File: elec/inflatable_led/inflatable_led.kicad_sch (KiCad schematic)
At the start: 87 parts, among them J1 Header-Male-2.54_1x20, J2 Conn_01x02_Pin, J3 Conn_01x02_Pin, SW1 TS-1093C-A7B2-D1, U1 RP2040, U2 W25Q128JVSIQTR, U3 TPS61165DRVR, U4 BQ24040DSQR, U5 AMS1117-3.3, U6 F.0603.00026/P2-0603B1TS2-06T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, U7 SI2323DS, X1 X322512MSB4SI

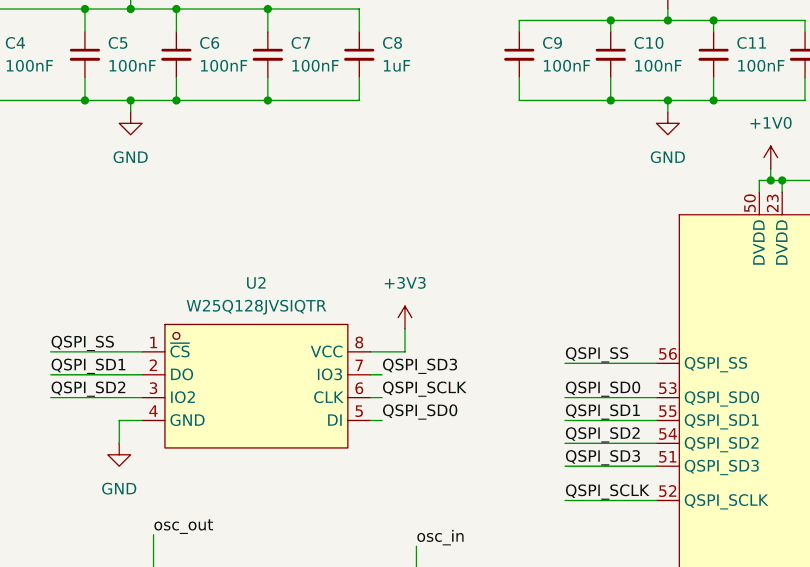
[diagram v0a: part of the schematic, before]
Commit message: fix missing 3.3V on flash
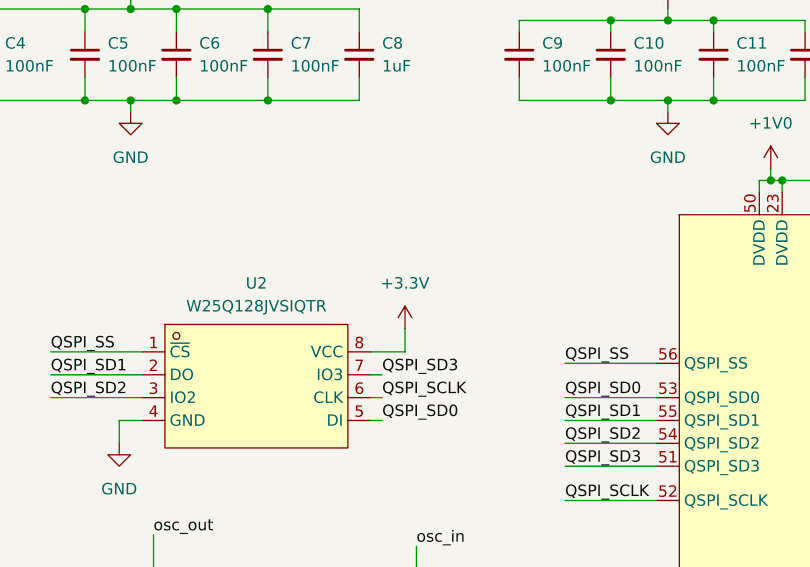
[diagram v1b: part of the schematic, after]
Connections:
- net +3V3 is gone; now on net +3.3V: U2.8 (VCC)
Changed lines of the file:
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@@
+	)
+	(symbol
+		(lib_id "power:+3.3V")
+		(at 85.09 62.23 0)
+		(unit 1)
+		(exclude_from_sim no)
+		(in_bom yes)
+		(on_board yes)
+		(dnp no)
+		(fields_autoplaced yes)
+		(property "Reference" "#PWR09"
+			(at 85.09 66.04 0)
+			(effects
+				(font
+					(size 1.27 1.27)
+				)
+				(hide yes)
+			)
+		)
+		(property "Value" "+3.3V"
+			(at 85.09 57.15 0)
+			(effects
+				(font
+					(size 1.27 1.27)
+				)
+			)
+		)
+		(property "Footprint" ""
+			(at 85.09 62.23 0)
+			(effects
+				(font
+					(size 1.27 1.27)
+				)
+				(hide yes)
+			)
+		)
+		(property "Datasheet" ""
+			(at 85.09 62.23 0)
+			(effects
+				(font
+					(size 1.27 1.27)
+				)
+				(hide yes)
+			)
+		)
+		(property "Description" "Power symbol creates a global label with name \"+3.3V\""
+			(at 85.09 62.23 0)
+			(effects
+				(font
+					(size 1.27 1.27)
+				)
+				(hide yes)
+			)
+		)
+		(pin "1"
+		)
+		(instances
+			(project "inflatable_led"
+				(path "/28d8f95b-9544-4a45-87c6-73291c5b1588"
+					(reference "#PWR09")
+					(unit 1)
+				)
+			)
+		)
 	)
 	(symbol
@@
 					(unit 1)
 				)
-			)
-		)
-	)
-	(symbol
-		(lib_id "power:+3V3")
-		(at 85.09 62.23 0)
-		(unit 1)
-		(exclude_from_sim no)
-		(in_bom yes)
-		(on_board yes)
-		(dnp no)
-		(fields_autoplaced yes)
-		(property "Reference" "#PWR09"
-			(at 85.09 66.04 0)
-			(effects
-				(font
-					(size 1.27 1.27)
-				)
-				(hide yes)
-			)
-		)
-		(property "Value" "+3V3"
-			(at 85.09 57.15 0)
-			(effects
-				(font
-					(size 1.27 1.27)
-				)
-			)
-		)
-		(property "Footprint" ""
-			(at 85.09 62.23 0)
-			(effects
-				(font
-					(size 1.27 1.27)
-				)
-				(hide yes)
-			)
-		)
-		(property "Datasheet" ""
-			(at 85.09 62.23 0)
-			(effects
-				(font
-					(size 1.27 1.27)
-				)
-				(hide yes)
-			)
-		)
-		(property "Description" "Power symbol creates a global label with name \"+3V3\""
-			(at 85.09 62.23 0)
-			(effects
-				(font
-					(size 1.27 1.27)
-				)
-				(hide yes)
-			)
-		)
-		(pin "1"
-		)
-		(instances
-			(project "inflatable_led"
-				(path "/28d8f95b-9544-4a45-87c6-73291c5b1588"
-					(reference "#PWR09")
-					(unit 1)
-				)

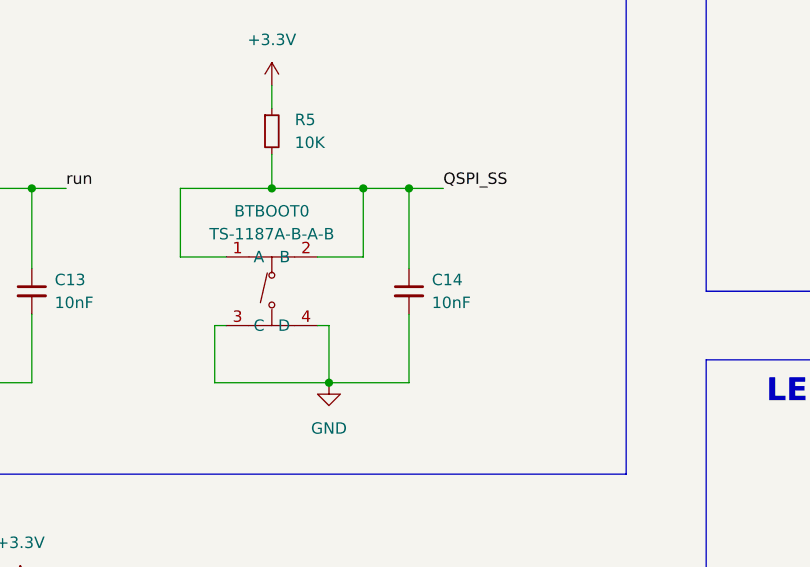
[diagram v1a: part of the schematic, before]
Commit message: v1 is working, add v2 requests
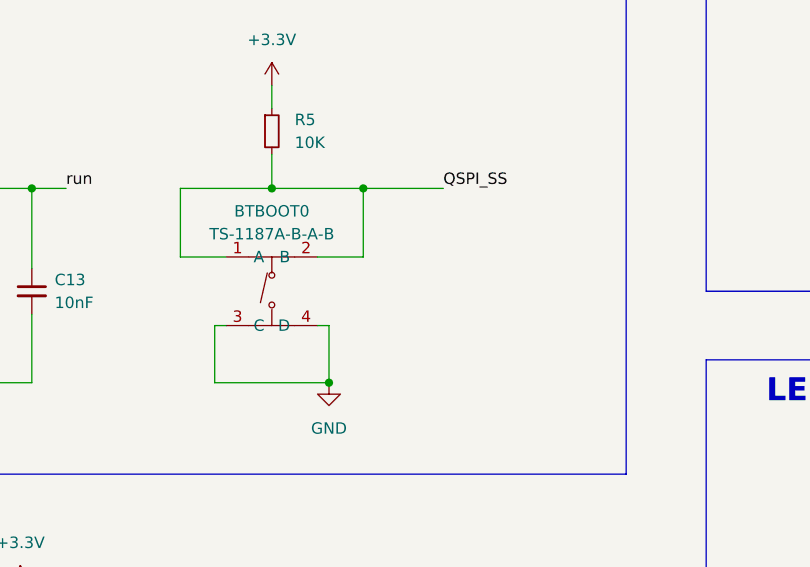
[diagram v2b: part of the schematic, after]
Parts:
- removed C14: 10nF, Capacitor_SMD:C_0402_1005Metric, symbol Device:C_Small
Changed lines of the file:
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@@
 	)
 	(junction
-		(at 181.61 179.07)
-		(diameter 0)
-		(color 0 0 0 0)
-	)
-	(junction
 		(at 157.48 45.72)
 		(diameter 0)
@@
 	(wire
 		(pts
-			(xy 181.61 193.04) (xy 181.61 200.66)
-		)
-		(stroke
-			(width 0)
-			(type default)
-		)
-	)
-	(wire
-		(pts
 			(xy 276.86 165.1) (xy 276.86 167.64)
 		)
@@
 	(wire
 		(pts
-			(xy 176.53 179.07) (xy 181.61 179.07)
+			(xy 176.53 179.07) (xy 185.42 179.07)
 		)
 		(stroke
@@
 	(wire
 		(pts
-			(xy 181.61 179.07) (xy 185.42 179.07)
-		)
-		(stroke
-			(width 0)
-			(type default)
-		)
-	)
-	(wire
-		(pts
 			(xy 102.87 77.47) (xy 113.03 77.47)
 		)
@@
 	(wire
 		(pts
-			(xy 181.61 200.66) (xy 172.72 200.66)
-		)
-		(stroke
-			(width 0)
-			(type default)
-		)
-	)
-	(wire
-		(pts
 			(xy 80.01 115.57) (xy 72.39 115.57)
 		)
@@
 	(wire
 		(pts
-			(xy 181.61 179.07) (xy 181.61 187.96)
-		)
-		(stroke
-			(width 0)
-			(type default)
-		)
-	)
-	(wire
-		(pts
 			(xy 189.23 130.81) (xy 195.58 130.81)
 		)
@@
 					(unit 1)
 				)
-			)
-		)
-	)
-	(symbol
-		(lib_id "Device:C_Small")
-		(at 181.61 190.5 0)
-		(unit 1)
-		(exclude_from_sim no)
-		(in_bom yes)
-		(on_board yes)
-		(dnp no)
-		(fields_autoplaced yes)
-		(property "Reference" "C14"
-			(at 184.15 189.2362 0)
-			(effects
-				(font
-					(size 1.27 1.27)
-				)
-				(justify left)
-			)
-		)
-		(property "Value" "10nF"
-			(at 184.15 191.7762 0)
-			(effects
-				(font
-					(size 1.27 1.27)
-				)
-				(justify left)
-			)
-		)
-		(property "Footprint" "Capacitor_SMD:C_0402_1005Metric"
-			(at 181.61 190.5 0)
-			(effects
-				(font
-					(size 1.27 1.27)
-				)
-				(hide yes)
-			)
-		)
-		(property "Datasheet" "~"
-			(at 181.61 190.5 0)
-			(effects
-				(font
-					(size 1.27 1.27)
-				)
-				(hide yes)
-			)
-		)
-		(property "Description" "Unpolarized capacitor, small symbol"
-			(at 181.61 190.5 0)
-			(effects
-				(font
-					(size 1.27 1.27)
-				)
-				(hide yes)
-			)
-		)
-		(property "LCSC Part" "C15195"
-			(at 181.61 190.5 0)
-			(effects
-				(font
-					(size 1.27 1.27)
-				)
-				(hide yes)
-			)
-		)
-		(pin "2"
-		)
-		(pin "1"
-		)
-		(instances
-			(project "inflatable_led"
-				(path "/28d8f95b-9544-4a45-87c6-73291c5b1588"
-					(reference "C14")
-					(unit 1)
-				)

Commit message: minor schematic changes
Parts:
- R12: now not fitted
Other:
- note added: "TODO: actually can't switch this"
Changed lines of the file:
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@@
 		)
 	)
+	(text "TODO: actually can't switch this"
+		(exclude_from_sim no)
+		(at 267.462 230.378 0)
+		(effects
+			(font
+				(size 1.27 1.27)
+			)
+		)
+	)
 	(text "LED ARE ONLY BEING POWERED FROM BATTERY, NOT USB"
 		(exclude_from_sim no)
@@
 		(in_bom yes)
 		(on_board yes)
-		(dnp no)
+		(dnp yes)
 		(fields_autoplaced yes)
 		(property "Reference" "R12"

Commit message: whole new circuit
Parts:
- removed BAT1, BAT2: BH-18650-A5BJ003, footprints:BAT-TH_BH-18650-A5BJ003, symbol local:BH-18650-A5BJ003
- removed C13: 10nF, Capacitor_SMD:C_0402_1005Metric, symbol Device:C_Small
- removed D8, D9: MBR0540T1G, footprints:SOD-123_L2.8-W1.8-LS3.7-RD, symbol local:MBR0540T1G
- removed J1: Header-Male-2.54_1x20, footprints:HDR-TH_20P-P2.54-V-M-1, symbol footprints:Header-Male-2.54_1x20
- removed SW1: TS-1093C-A7B2-D1, footprints:SW-TH_TS-1093C-A7B3-D1, symbol local:TS-1093C-A7B2-D1
- removed TP_POWER_OR_1: TestPoint, TestPoint:TestPoint_Pad_D1.5mm, symbol Connector:TestPoint
- removed U4: BQ24040DSQR, footprints:WSON-10_L2.0-W2.0-P0.40-BL-EP, symbol local:BQ24040DSQR
- removed U5: AMS1117-3.3, footprints:SOT-223-3_L6.5-W3.4-P2.30-LS7.0-BR, symbol footprints:AMS1117-3.3
- added BT1: BH-18650-B1BA007, footprints:BAT-SMD_BH-18650-B1BA007, symbol local:BH-18650-B1BA007
- added BTBOOT1, BTUI1: TS-1187A-B-A-B, footprints:SW-SMD_4P-L5.1-W5.1-P3.70-LS6.5-TL-2, symbol footprints:TS-1187A-B-A-B
- added C14: 47nF, Capacitor_SMD:C_0603_1608Metric, symbol Device:C_Small
- added C23, C24: 10uF, Capacitor_SMD:C_0805_2012Metric, symbol Device:C_Small
- added C25, C26: 1uF, Capacitor_SMD:C_0603_1608Metric, symbol Device:C_Small
- added CN1: S2B-PH-SM4-TB(LF)(SN), footprints:CONN-SMD_P2.00_S2B-PH-SM4-TB-LF-SN, symbol local:S2B-PH-SM4-TB(LF)(SN)
- added J1: Conn_01x10, Connector_PinHeader_1.00mm:PinHeader_1x10_P1.00mm_Vertical, symbol Connector_Generic:Conn_01x10
- added J4: USB4205-GF-A_REVA, footprints:GCT_USB4205-GF-A_REVA, symbol local:USB4205-GF-A_REVA
- added JP1: SolderJumper_3_Bridged12, Jumper:SolderJumper-3_P1.3mm_Bridged12_RoundedPad1.0x1.5mm, symbol Jumper:SolderJumper_3_Bridged12
- added JP2: SolderJumper_2_Open, Jumper:SolderJumper-2_P1.3mm_Open_TrianglePad1.0x1.5mm, symbol Jumper:SolderJumper_2_Open
- added JP3: SolderJumper_3_Open, Jumper:SolderJumper-3_P2.0mm_Open_TrianglePad1.0x1.5mm, symbol Jumper:SolderJumper_3_Open
- added L2: 1uH/3A, Inductor_SMD:L_1008_2520Metric, symbol Device:L_Small
- added Q1: 2N7002KW_R1_00001, footprints:SOT-323-3_L2.0-W1.3-P1.30-LS2.1-BR, symbol local:2N7002KW_R1_00001
- added R17, R18, R20: 10K, Resistor_SMD:R_0402_1005Metric, symbol Device:R_Small
- added R19: 10k, Resistor_SMD:R_0603_1608Metric, symbol Device:R_Small
- added TP1, TP2, TP7, TP8: TestPoint, TestPoint:TestPoint_Pad_D1.0mm, symbol Connector:TestPoint
- added U4: BQ25601DRTWR, footprints:WQFN-24_L4.0-W4.0-P0.50-TL-EP2.7, symbol local:BQ25601DRTWR
- added U5: STM6601GU2BDM6F, Package_DFN_QFN:TDFN-12_2x3mm_P0.5mm, symbol sternenbauer:SRC0
- added U8: TPS7A0233DQNR, footprints:X2SON-4_L1.0-W1.0-P0.65-TL-EP, symbol local:TPS7A0233DQNR
- C19: value 1uF -> 0.1uF; footprint Capacitor_SMD:C_0805_2012Metric -> Capacitor_SMD:C_0603_1608Metric; Digikey (none) -> 311-1776-1-ND; LCSC Part C28323 -> (none)
- C20, C21: value 100nF -> 1uF; footprint Capacitor_SMD:C_0402_1005Metric -> Capacitor_SMD:C_0805_2012Metric; LCSC Part C1525 -> C28323
- R7: value 600R -> 10K; LCSC Part C2076855 -> C25744
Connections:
- net CHG_CHG is gone; now on net CHG_STAT: LED_CHG_2.1 (K)
- net +3.3V: now also J1.2 (Pin_2), R19.1, U8.1 (OUT)
- net +BATT: now also BT1.1, BT1.3, CN1.1, J1.3 (Pin_3), JP1.3 (B), U4.13 (BAT), U4.14 (BAT); no longer C19.1, R8.1, R9.1, U7.2 (S)
- net CHG_PG: now also U1.9 (GPIO7), U4.3 (~{PG})
- net DIM_CTRL: now also U1.2 (GPIO0); no longer U1.6 (GPIO4)
- net GND: now also BT1.2, BT1.4, BTBOOT1.3 (C), BTBOOT1.4 (D), BTUI1.1 (A), BTUI1.2 (B), C23.2, C24.2, C25.2, C26.2, CN1.2, CN1.3, CN1.4, J1.1 (Pin_1), J4.A1 (GND_A), J4.A12 (GND_A__1), J4.B1 (GND_B), J4.B12 (GND_B__1), J4.SH1 (SHIELD), J4.SH2 (SHIELD__1), J4.SH3 (SHIELD__2), J4.SH4 (SHIELD__3), Q1.2 (S), R17.2, R20.2, U4.17 (GND), U4.18 (GND), U4.25 (EP), U4.9 (~{CE}), U5.12 (GND), U8.2 (GND), U8.5 (GND); no longer R7.2
- net LED_ON: now also R16.1, TP_LED_ON1.1, U1.3 (GPIO1); no longer R16.2, U1.5 (GPIO3)
- net USB_CC1: now also J4.A5 (CC1)
- net USB_CC2: now also J4.B5 (CC2)
- net USB_DM: now also J4.A7 (DN1), J4.B7 (DN2)
- net USB_DP: now also J4.A6 (DP1), J4.B6 (DP2)
- net VBUS: now also J1.5 (Pin_5), J4.A4 (VBUS_A), J4.A9 (VBUS_A__1), J4.B4 (VBUS_B), J4.B9 (VBUS_B__1), U4.1 (VBUS), U4.2 (PSEL), U4.24 (VAC)
- net CHG_REGN: now reaches R7.1
- net CHG_REGN: now also U4.22 (REGN)
- net GPIO8: now reaches U1.11 (GPIO8)
- net GPIO8: now also J1.7 (Pin_7)
- net GPIO9: now reaches U1.12 (GPIO9)
- net GPIO9: now also J1.8 (Pin_8)
- net GPIO10: now reaches U1.13 (GPIO10)
- net GPIO10: now also J1.9 (Pin_9)
- net GPIO11: now reaches U1.14 (GPIO11)
- net GPIO11: now also J1.10 (Pin_10)
- net GPIO12: now reaches U1.15 (GPIO12)
- net GPIO13: now reaches U1.16 (GPIO13)
- net PWR_HOLD: now reaches U1.17 (GPIO14)
- net PWR_HOLD: now also TP2.1, U5.4 (PSHOLD)
- net PWR_LOW: now reaches U1.18 (GPIO15)
- net PWR_LOW: now also R19.2, U5.7 (VCCLO)
- net BTN1: now reaches U1.27 (GPIO16)
- net BTN1: now also JP2.2 (B), U5.8 (PBOUT)
- net CHG_QON: now reaches U1.4 (GPIO2)
- net CHG_QON: now also U4.12 (~{QON})
- net CHG_STAT: now reaches U1.8 (GPIO6)
- net CHG_STAT: now also U4.4 (STAT)
- net ON_OFF_BT renamed PWR_ON
- net PWR_ON: now also BTUI1.3 (C), BTUI1.4 (D), JP2.1 (A), JP3.1 (A), U5.6 (PB); no longer U1.7 (GPIO5)
- net POWER_IN_OR renamed VCC
- net VCC: now also C19.1, R8.1, R9.1, C23.1, J1.4 (Pin_4), JP1.1 (A), L2.2, U4.15 (SYS), U4.16 (SYS), U5.1 (VCC), U8.4 (IN)
- new net: C14.2, L2.1, U4.19 (SW), U4.20 (SW)
- new net: C14.1, U4.21 (BTST)
- new net: BTBOOT1.1 (A), BTBOOT1.2 (B), JP3.3 (B)
- new net: Q1.1 (G), R16.2, R20.1
- new net: Q1.3 (D), R18.2, U7.1 (G)
- new net: C25.1, U5.5 (CSRD)
- new net: R17.1, R7.2, U4.11 (TS)
- new net: C24.1, U4.23 (PMID)
- new net: JP1.2 (C), R18.1, U7.2 (S)
- new net: C26.1, U5.3 (VREF)
- new net CHG_INT: U1.5 (GPIO3), U4.7 (~{INT})
- new net PWR_EN: J1.6 (Pin_6), TP1.1, U5.9 (EN), U8.3 (EN)
- new net PWR_INT: TP8.1, U5.11 (INT)
- new net PWR_RESET: TP7.1, U5.10 (RST)
- new net PWR_SR: JP3.2 (C), U5.2 (SR)
- new net SCL: U1.7 (GPIO5), U4.5 (SCL)
- new net SDA: U1.6 (GPIO4), U4.6 (SDA)
- no-connect marks 0 -> 18
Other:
- note added: "Capacitor at CSRD defines a timeout of 10s for long presses (PB+SR) that will deassert EN and shutdown the device."
- note added: "Check polarity before plugging in."
- note added: "Making sure we can actuate smart reset together with PB pin if necessary."
- note added: "ON OFF CONTROLLER"
- note added: "VCC must be min. 3.5V for EN to go high. Also a 32ms drop below 3.3V will make EN go low. VCCLO goes low anytime VCC falls below 3.5V. Power must be confirmed within 1.4s after the button has been pressed."
- note removed: "POWER OR"
- note removed: "TODO: actually can't switch this"
- moved on the sheet: BTBOOT0, BTRESET1, C1, C18, C2, C22, J3, LED_CHG_2, LED_PG_1, R1, R12, R13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

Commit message: update bom
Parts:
- C14: LCSC Part (none) -> C77012
- C19: value 0.1uF -> 100nF; footprint Capacitor_SMD:C_0603_1608Metric -> Capacitor_SMD:C_0402_1005Metric; LCSC Part (none) -> C1525
- C23, C24: LCSC Part (none) -> C15850
- C25, C26: footprint Capacitor_SMD:C_0603_1608Metric -> Capacitor_SMD:C_0805_2012Metric; LCSC Part (none) -> C28323
- D3, D4, D5, D6, D7: LCSC Part (none) -> C5220764
- H1, H2, H3, H4, J4: now not fitted
- J1: now not fitted; now left out of the parts list
- J2: now left out of the parts list
- L2: LCSC Part (none) -> C435392
- R19: footprint Resistor_SMD:R_0603_1608Metric -> Resistor_SMD:R_0402_1005Metric; LCSC Part (none) -> C25744
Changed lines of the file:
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@@
 			)
 		)
+		(property "LCSC Part" "C435392"
+			(at 299.72 134.62 0)
+			(effects
+				(font
+					(size 1.27 1.27)
+				)
+				(hide yes)
+			)
+		)
 		(pin "2"
 		)
@@
 			)
 		)
+		(property "LCSC Part" "C77012"
+			(at 288.29 132.08 0)
+			(effects
+				(font
+					(size 1.27 1.27)
+				)
+				(hide yes)
+			)
+		)
 		(pin "2"
 		)
@@
 		(in_bom no)
 		(on_board yes)
-		(dnp no)
+		(dnp yes)
 		(fields_autoplaced yes)
 		(property "Reference" "H2"
@@
 			)
 		)
+		(property "LCSC Part" "C5220764"
+			(at 370.84 41.91 0)
+			(effects
+				(font
+					(size 1.27 1.27)
+				)
+				(hide yes)
+			)
+		)
 		(pin "1"
 		)
@@
 			)
 		)
-		(property "Footprint" "Resistor_SMD:R_0603_1608Metric"
+		(property "Footprint" "Resistor_SMD:R_0402_1005Metric"
 			(at 410.21 219.71 0)
 			(effects
@@
 			)
 		)
+		(property "LCSC Part" "C25744"
+			(at 410.21 219.71 0)
+			(effects
+				(font
+					(size 1.27 1.27)
+				)
+				(hide yes)
+			)
+		)
 		(pin "2"
 		)
@@
 			)
 		)
-		(property "Footprint" "Capacitor_SMD:C_0603_1608Metric"
+		(property "Footprint" "Capacitor_SMD:C_0805_2012Metric"
 			(at 367.03 231.14 0)
 			(effects
@@
 			)
 		)
+		(property "LCSC Part" "C28323"
+			(at 367.03 231.14 0)
+			(effects
+				(font
+					(size 1.27 1.27)
+				)
+				(hide yes)
+			)
+		)
 		(pin "2"
 		)
@@
 		(unit 1)
 		(exclude_from_sim no)
-		(in_bom yes)
+		(in_bom no)
 		(on_board yes)
-		(dnp no)
+		(dnp yes)
 		(fields_autoplaced yes)
 		(property "Reference" "J1"
@@
 		(in_bom yes)
 		(on_board yes)
-		(dnp no)
+		(dnp yes)
 		(fields_autoplaced yes)
 		(property "Reference" "J4"
@@
 			)
 		)
+		(property "LCSC Part" "C5220764"
+			(at 370.84 82.55 0)
+			(effects
+				(font
+					(size 1.27 1.27)
+				)
+				(hide yes)
+			)
+		)
 		(pin "1"
 		)
@@
 			)
 		)
+		(property "LCSC Part" "C5220764"
+			(at 370.84 72.39 0)
+			(effects
+				(font
+					(size 1.27 1.27)
+				)
+				(hide yes)
+			)
+		)
 		(pin "1"
 		)
@@
 			)
 		)
-		(property "LCSC Part" ""
+		(property "LCSC Part" "C15850"
 			(at 316.23 138.43 0)
 			(effects
@@
 			)
 		)
+		(property "LCSC Part" "C5220764"
+			(at 370.84 62.23 0)
+			(effects
+				(font
+					(size 1.27 1.27)
+				)
+				(hide yes)
+			)
+		)
 		(pin "1"
 		)
@@
 		(unit 1)
 		(exclude_from_sim no)
-		(in_bom yes)
+		(in_bom no)
 		(on_board yes)
 		(dnp yes)
@@
 		(in_bom no)
 		(on_board yes)
-		(dnp no)
+		(dnp yes)
 		(fields_autoplaced yes)
 		(property "Reference" "H1"
@@
 			)
 		)
+		(property "LCSC Part" "C5220764"
+			(at 370.84 52.07 0)
+			(effects
+				(font
+					(size 1.27 1.27)
+				)
+				(hide yes)
+			)
+		)
 		(pin "1"
 		)
@@
 			)
 		)
-		(property "Value" "0.1uF"
+		(property "Value" "100nF"
 			(at 356.87 232.4162 0)
 			(effects
@@
 			)
 		)
-		(property "Footprint" "Capacitor_SMD:C_0603_1608Metric"
+		(property "Footprint" "Capacitor_SMD:C_0402_1005Metric"
 			(at 354.33 231.14 0)
 			(effects
@@
 			)
 		)
+		(property "LCSC Part" "C1525"
+			(at 354.33 231.14 0)
+			(effects
+				(font
+					(size 1.27 1.27)
+				)
+				(hide yes)
+			)
+		)
 		(pin "2"
 		)
@@
 			)
 		)
-		(property "LCSC Part" ""
+		(property "LCSC Part" "C15850"
 			(at 306.07 138.43 0)
 			(effects
@@
 		(in_bom no)
 		(on_board yes)
-		(dnp no)
+		(dnp yes)
 		(fields_autoplaced yes)
 		(property "Reference" "H3"
@@
 		(in_bom no)
 		(on_board yes)
-		(dnp no)
+		(dnp yes)
 		(fields_autoplaced yes)
 		(property "Reference" "H4"
@@
 			)
 		)
-		(property "Footprint" "Capacitor_SMD:C_0603_1608Metric"
+		(property "Footprint" "Capacitor_SMD:C_0805_2012Metric"
 			(at 407.67 231.14 0)
 			(effects
@@
 			(at 407.67 231.14 0)
 			(effects
+				(font
+					(size 1.27 1.27)
+				)
+				(hide yes)
+			)
+		)
+		(property "LCSC Part" "C28323"
+			(at 407.67 231.14 0)
+			(effects

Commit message: fix additional parts in BOM
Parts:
- C14: footprint Capacitor_SMD:C_0603_1608Metric -> Capacitor_SMD:C_0402_1005Metric; LCSC Part C77012 -> C272875
- D1: LCSC Part C21353 -> C109213
- R12: now fitted
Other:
- moved on the sheet: C15, C16, C17, D1, L1, R6, TP_DIM_CTRL_1, U3

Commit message: final tweaks
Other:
- note added: "MOUNTING HOLES"
- moved on the sheet: BTBOOT1, C10, C11, C12, C14, C18, C19, C20, C21, C23, C24, C25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

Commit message: dnp battery conn
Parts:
- CN1: now not fitted
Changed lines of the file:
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@@
 		(in_bom yes)
 		(on_board yes)
-		(dnp no)
+		(dnp yes)
 		(fields_autoplaced yes)
 		(property "Reference" "CN1"
